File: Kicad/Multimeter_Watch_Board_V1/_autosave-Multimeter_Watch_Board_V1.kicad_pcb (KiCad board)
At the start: 4 copper layers, 5 parts, among them J1 AudioJack3_Ground_renamedPins, J2 AudioJack3_Ground_renamedPins, J3 AudioJack3_Ground_renamedPins, J4 Conn_01x16_Female, J5 Conn_01x16_Female

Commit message: clear board before next attempt, resize to 55x46.4mm to fit battery
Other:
- board outline added: 55 x 46 mm
- board text added: "Battery length"
- board text added: "Battery width"
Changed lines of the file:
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@@
   (general
     (thickness 1.6)
-    (drawings 4)
+    (drawings 14)
     (tracks 1)
     (zones 0)
@@
     )
   )
+  (dimension 2.125 (width 0.15) (layer Dwgs.User)
+    (gr_text "2.125 mm" (at 90.7 48.9375 270) (layer Dwgs.User)
+      (effects (font (size 1 1) (thickness 0.15)))
+    )
+    (feature1 (pts (xy 106.2 50) (xy 91.413579 50)))
+    (feature2 (pts (xy 106.2 47.875) (xy 91.413579 47.875)))
+    (crossbar (pts (xy 92 47.875) (xy 92 50)))
+    (arrow1a (pts (xy 92 50) (xy 91.413579 48.873496)))
+    (arrow1b (pts (xy 92 50) (xy 92.586421 48.873496)))
+    (arrow2a (pts (xy 92 47.875) (xy 91.413579 49.001504)))
+    (arrow2b (pts (xy 92 47.875) (xy 92.586421 49.001504)))
+  )
+  (dimension 46 (width 0.15) (layer Dwgs.User)
+    (gr_text "46.000 mm" (at 167.8 73 270) (layer Dwgs.User)
+      (effects (font (size 1 1) (thickness 0.15)))
+    )
+    (feature1 (pts (xy 151 96) (xy 167.086421 96)))
+    (feature2 (pts (xy 151 50) (xy 167.086421 50)))
+    (crossbar (pts (xy 166.5 50) (xy 166.5 96)))
+    (arrow1a (pts (xy 166.5 96) (xy 165.913579 94.873496)))
+    (arrow1b (pts (xy 166.5 96) (xy 167.086421 94.873496)))
+    (arrow2a (pts (xy 166.5 50) (xy 165.913579 51.126504)))
+    (arrow2b (pts (xy 166.5 50) (xy 167.086421 51.126504)))
+  )
+  (gr_line (start 155 96) (end 151 96) (layer Edge.Cuts) (width 0.05))
+  (gr_line (start 155 50) (end 155 96) (layer Edge.Cuts) (width 0.05))
+  (gr_line (start 100 96) (end 151 96) (layer Edge.Cuts) (width 0.05))
+  (gr_line (start 100 50) (end 100 96) (layer Edge.Cuts) (width 0.05))
+  (gr_text "Battery length\n" (at 126.6 101.1) (layer Dwgs.User)
+    (effects (font (size 1 1) (thickness 0.15)))
+  )
+  (dimension 46.4 (width 0.15) (layer Dwgs.User)
+    (gr_text "46.400 mm" (at 126.6 103.6) (layer Dwgs.User)
+      (effects (font (size 1 1) (thickness 0.15)))
+    )
+    (feature1 (pts (xy 149.8 85.3) (xy 149.8 102.886421)))
+    (feature2 (pts (xy 103.4 85.3) (xy 103.4 102.886421)))
+    (crossbar (pts (xy 103.4 102.3) (xy 149.8 102.3)))
+    (arrow1a (pts (xy 149.8 102.3) (xy 148.673496 102.886421)))
+    (arrow1b (pts (xy 149.8 102.3) (xy 148.673496 101.713579)))
+    (arrow2a (pts (xy 103.4 102.3) (xy 104.526504 102.886421)))
+    (arrow2b (pts (xy 103.4 102.3) (xy 104.526504 101.713579)))
+  )
+  (gr_text "Battery width" (at 94.7 78.9 270) (layer Dwgs.User)
+    (effects (font (size 1 1) (thickness 0.15)))
+  )
+  (dimension 34.1 (width 0.15) (layer Dwgs.User)
+    (gr_text "34.100 mm" (at 92 78.85 270) (layer Dwgs.User)
+      (effects (font (size 1 1) (thickness 0.15)))
+    )
+    (feature1 (pts (xy 121.4 95.9) (xy 92.713579 95.9)))
+    (feature2 (pts (xy 121.4 61.8) (xy 92.713579 61.8)))
+    (crossbar (pts (xy 93.3 61.8) (xy 93.3 95.9)))
+    (arrow1a (pts (xy 93.3 95.9) (xy 92.713579 94.773496)))
+    (arrow1b (pts (xy 93.3 95.9) (xy 93.886421 94.773496)))
+    (arrow2a (pts (xy 93.3 61.8) (xy 92.713579 62.926504)))
+    (arrow2b (pts (xy 93.3 61.8) (xy 93.886421 62.926504)))
+  )
   (dimension 0.5 (width 0.15) (layer Dwgs.User)

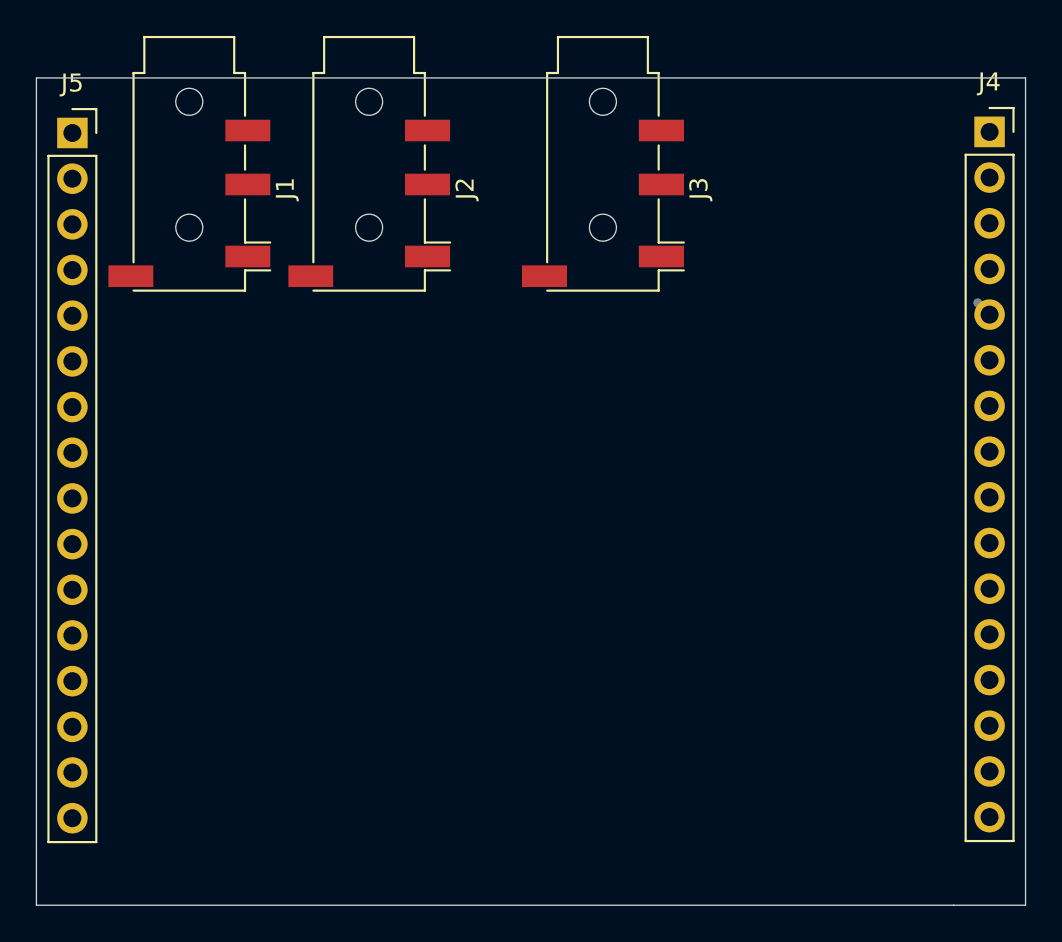
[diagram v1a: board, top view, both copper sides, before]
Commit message: second layout attempt, various pinout changes for better routing
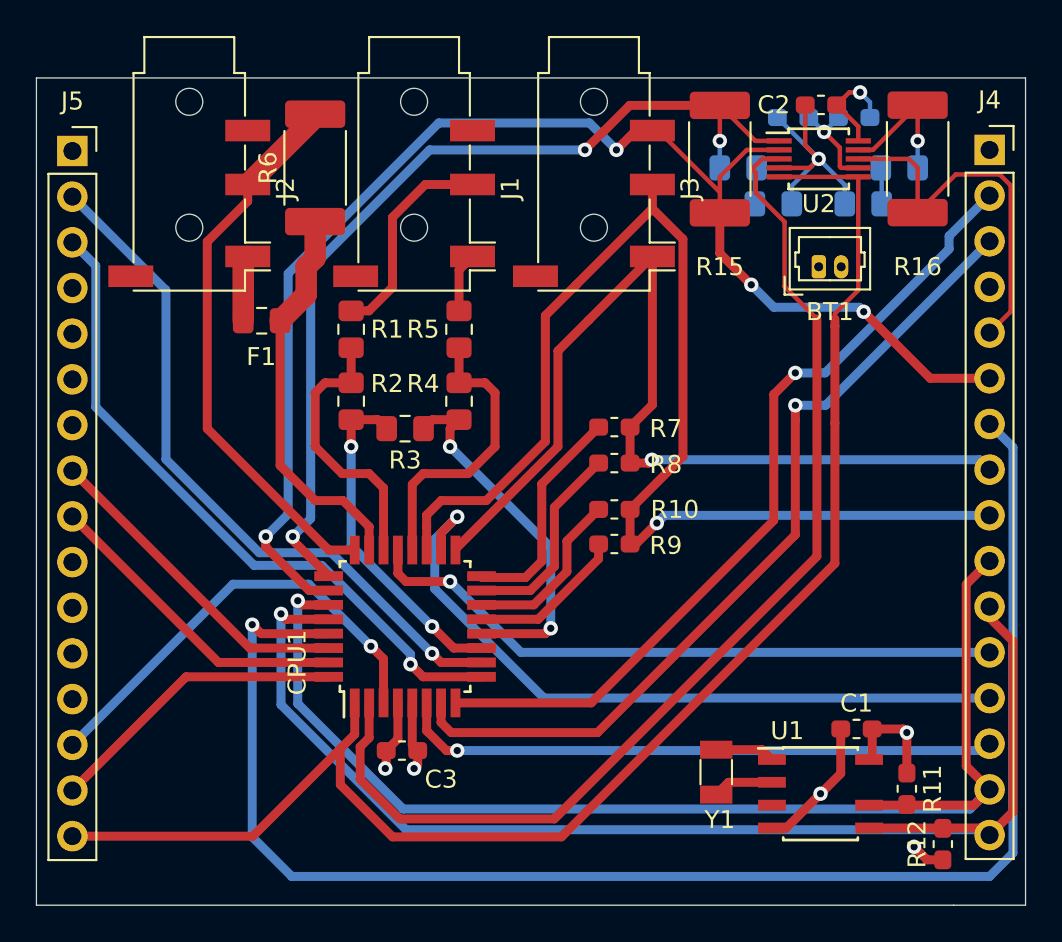
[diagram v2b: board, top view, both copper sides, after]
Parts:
- added BT1: Some Li-Po?, Connector_Molex:Molex_PicoBlade_53047-0210_1x02_P1.25mm_Vertical, F.Cu at (143.5, 60.5)
- added C1: 100n, Capacitor_SMD:C_0603_1608Metric_Pad1.05x0.95mm_HandSolder, F.Cu at (145.6, 86.2)
- added C2: 100n, Capacitor_SMD:C_0603_1608Metric_Pad1.05x0.95mm_HandSolder, F.Cu at (143.6, 51.5)
- added C3: 100n, Capacitor_SMD:C_0603_1608Metric_Pad1.05x0.95mm_HandSolder, F.Cu at (120.3, 87.4)
- added C4: C_Small, Capacitor_SMD:C_0805_2012Metric_Pad1.15x1.40mm_HandSolder, B.Cu at (141.0, 57.0)
- added C5: C_Small, Capacitor_SMD:C_0805_2012Metric_Pad1.15x1.40mm_HandSolder, B.Cu at (146.0, 57.0)
- added CPU1: LGT8F328P-QFP32L, Package_QFP:TQFP-32_7x7mm_P0.8mm, F.Cu at (120.5, 80.5)
- added F1: Fuse, Fuse:Fuse_0805_2012Metric_Pad1.15x1.40mm_HandSolder, F.Cu at (112.5, 63.5)
- added R1: R, Resistor_SMD:R_0805_2012Metric_Pad1.15x1.40mm_HandSolder, F.Cu at (117.5, 64.0)
- added R10: 680, Resistor_SMD:R_0603_1608Metric_Pad1.05x0.95mm_HandSolder, F.Cu at (132.1, 74.0)
- added R11: R, Resistor_SMD:R_0603_1608Metric_Pad1.05x0.95mm_HandSolder, F.Cu at (148.4, 89.5)
- added R12: R, Resistor_SMD:R_0603_1608Metric_Pad1.05x0.95mm_HandSolder, F.Cu at (150.4, 92.6)
- added R13: 1M, Resistor_SMD:R_0603_1608Metric_Pad1.05x0.95mm_HandSolder, B.Cu at (145.5, 52.2)
- added R14: 1M, Resistor_SMD:R_0603_1608Metric_Pad1.05x0.95mm_HandSolder, B.Cu at (142.1, 52.2)
- added R15: R, Resistor_SMD:R_2512_6332Metric_Pad1.52x3.35mm_HandSolder, F.Cu at (138.0, 54.5)
- added R16: 30, Resistor_SMD:R_2512_6332Metric_Pad1.52x3.35mm_HandSolder, F.Cu at (149.0, 54.5)
- added R17: R_Small, Resistor_SMD:R_0805_2012Metric_Pad1.15x1.40mm_HandSolder, B.Cu at (139.0, 55.0)
- added R18: R_Small, Resistor_SMD:R_0805_2012Metric_Pad1.15x1.40mm_HandSolder, B.Cu at (148.0, 55.0)
- added R2: R, Resistor_SMD:R_0805_2012Metric_Pad1.15x1.40mm_HandSolder, F.Cu at (117.5, 68.0)
- added R3: R, Resistor_SMD:R_0805_2012Metric_Pad1.15x1.40mm_HandSolder, F.Cu at (120.5, 69.5)
- added R4: R, Resistor_SMD:R_0805_2012Metric_Pad1.15x1.40mm_HandSolder, F.Cu at (123.5, 68.0)
- added R5: R, Resistor_SMD:R_0805_2012Metric_Pad1.15x1.40mm_HandSolder, F.Cu at (123.5, 64.0)
- added R6: R_shunt, Resistor_SMD:R_2512_6332Metric_Pad1.52x3.35mm_HandSolder, F.Cu at (115.5, 55.0)
- added R7: 470k, Resistor_SMD:R_0603_1608Metric_Pad1.05x0.95mm_HandSolder, F.Cu at (132.1, 69.4)
- added R8: 680, Resistor_SMD:R_0603_1608Metric_Pad1.05x0.95mm_HandSolder, F.Cu at (132.1, 71.4)
- added R9: 470k, Resistor_SMD:R_0603_1608Metric_Pad1.05x0.95mm_HandSolder, F.Cu at (132.1, 75.9)
- added U1: PCF85163-SO08, Package_SO:SOIC-8-N7_3.9x4.9mm_P1.27mm, F.Cu at (143.6, 89.8)
- added U2: AD8592, Package_SO:MSOP-10_3x3mm_P0.5mm, F.Cu at (143.5, 54.5)
- added Y1: 32kHz, Crystal:Crystal_SMD_3215-2Pin_3.2x1.5mm, F.Cu at (137.8, 88.6)
- moved J1 12.5 mm to (121.0, 56.1)
- moved J2 10.0 mm to (108.5, 56.1)
- moved J4 1.00 mm to (153.0, 54.0)
- moved J5 1.00 mm to (102.0, 54.1)
- moved J3 0.50 mm to (131.0, 56.1)
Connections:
- net /ADC2 renamed Net-(J2-Pad2)
- J2 pad 3: Net-(F1-Pad1) (its old number) -> /ADC1
- J3 pad 2: /ADC7 -> /ADC3
- J3 pad 4: /ADC1 -> /ADC11
- J4 pad 10: /SDA -> /SCL
- J4 pad 11: /SCL -> /SDA
- J4 pad 14: /BUTT3 -> /PE5
- J4 pad 15: /SDA -> /SCL
- J4 pad 16: /SCL -> /SDA
- J4 pad 2: /BUTT2 -> /PB7
- J4 pad 3: /BUTT1 -> /PB6
- J4 pad 6: /ADC1 -> /ADC3
- J4 pad 8: /ADC6 -> /ADC11
- J4 pad 9: /ADC7 -> /ADC6
- J5 pad 14: /BUTT6 -> /PE4
- J5 pad 15: /PB0 -> /PD2
- J5 pad 16: /PE4 -> /PD3
- J5 pad 2: /BUTT4 -> /PD6
- J5 pad 3: /BUTT5 -> /PD5
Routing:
- net /RESET: track 0.00 -> 84.4 mm, vias 0 -> 1
- net /PD3: track 0.00 -> 83.2 mm
- net /ADC3: track 0.00 -> 76.2 mm, vias 0 -> 4
- net /SDA: track 0.00 -> 70.9 mm, vias 0 -> 1
- net /SCL: track 0.00 -> 69.7 mm, vias 0 -> 1
- net /ADC6: track 0.00 -> 68.7 mm, vias 0 -> 1
- net /PD4: track 0.00 -> 61.6 mm
- net /ADC11: track 0.00 -> 53.2 mm, vias 0 -> 1
- net /ADC2: track 0.00 -> 52.4 mm, vias 0 -> 3
- net /PB6: track 0.00 -> 47.9 mm, vias 0 -> 1
- net /PB7: track 0.00 -> 46.5 mm, vias 0 -> 1
- net /SWC: track 0.00 -> 40.1 mm, vias 0 -> 1
- net /PD6: track 0.00 -> 39.0 mm, vias 0 -> 1
- net /PD5: track 0.00 -> 37.7 mm, vias 0 -> 1
- net /SWD: track 0.00 -> 36.0 mm, vias 0 -> 1
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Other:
- board text removed: "Battery length"
- board text removed: "Battery width"
